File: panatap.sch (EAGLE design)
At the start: 23 parts, among them Q1 J310, Q2 BFS17, X1 IF_IN, X2 RF_OUT

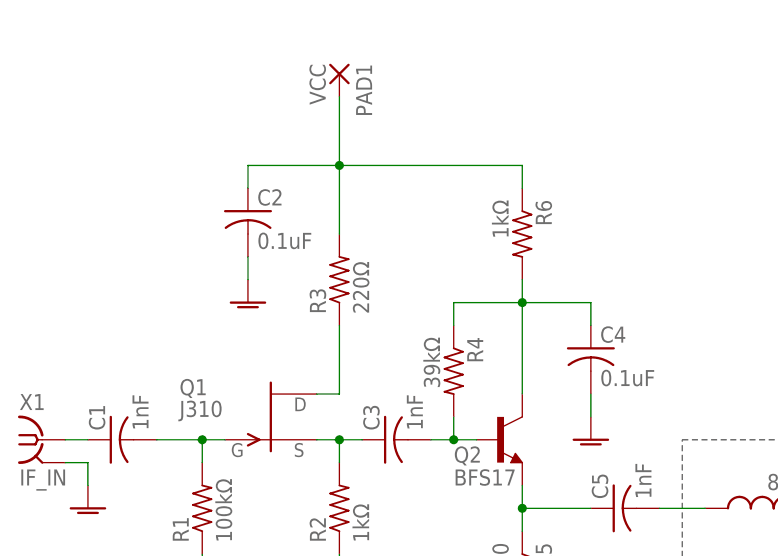
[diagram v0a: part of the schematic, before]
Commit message: Updated schematic and board with revised capacitor placement
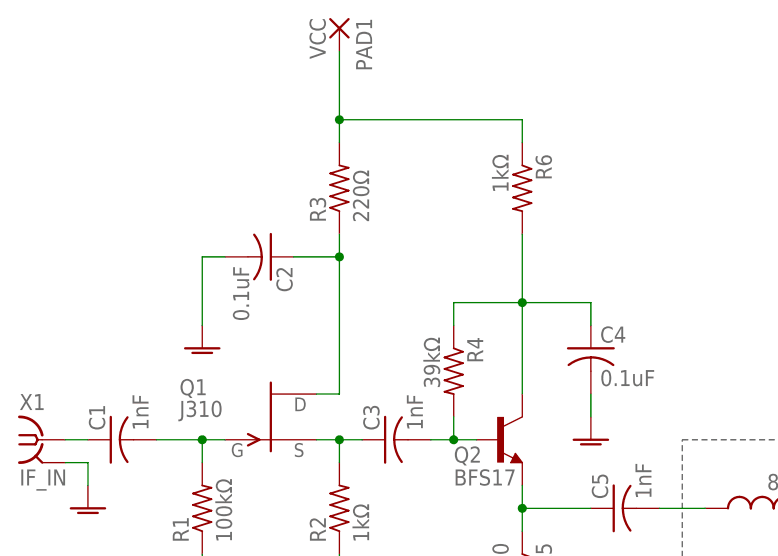
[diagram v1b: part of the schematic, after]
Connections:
- net N$8: no longer C2.1
- net N$9: now also C2.1
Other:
- moved on the sheet: C2, PAD1, R3, R6
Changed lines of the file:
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@@
 <instance part="C5" gate="G$1" x="76.2" y="45.72" rot="R90"/>
 <instance part="GND1" gate="1" x="30.48" y="35.56" smashed="yes"/>
-<instance part="PAD1" gate="G$1" x="45.72" y="93.98" rot="R270"/>
-<instance part="R3" gate="G$1" x="45.72" y="71.12" rot="R90"/>
-<instance part="C2" gate="G$1" x="35.56" y="78.74"/>
-<instance part="GND2" gate="1" x="35.56" y="68.58" smashed="yes"/>
+<instance part="PAD1" gate="G$1" x="45.72" y="99.06" rot="R270"/>
+<instance part="R3" gate="G$1" x="45.72" y="81.28" rot="R90"/>
+<instance part="C2" gate="G$1" x="38.1" y="73.66" rot="R270"/>
+<instance part="GND2" gate="1" x="30.48" y="63.5" smashed="yes"/>
 <instance part="C4" gate="G$1" x="73.66" y="63.5"/>
 <instance part="R4" gate="G$1" x="58.42" y="60.96" rot="R270"/>
 <instance part="GND3" gate="1" x="73.66" y="53.34" smashed="yes"/>
 <instance part="GND4" gate="1" x="45.72" y="35.56" smashed="yes"/>
-<instance part="R6" gate="G$1" x="66.04" y="76.2" rot="R270"/>
+<instance part="R6" gate="G$1" x="66.04" y="81.28" rot="R270"/>
 <instance part="R5" gate="G$1" x="66.04" y="38.1" rot="R270"/>
 <instance part="GND5" gate="1" x="66.04" y="27.94" smashed="yes"/>
@@
 <net name="GNDA" class="0">
 <segment>
-<pinref part="C2" gate="G$1" pin="2"/>
-<pinref part="GND2" gate="1" pin="GNDA"/>
-<wire x1="35.56" y1="73.66" x2="35.56" y2="71.12" width="0.1524" layer="91"/>
-</segment>
-<segment>
 <pinref part="GND3" gate="1" pin="GNDA"/>
 <pinref part="C4" gate="G$1" pin="2"/>
@@
 <wire x1="144.78" y1="33.02" x2="144.78" y2="35.56" width="0.1524" layer="91" style="longdash"/>
 </segment>
+<segment>
+<pinref part="C2" gate="G$1" pin="2"/>
+<pinref part="GND2" gate="1" pin="GNDA"/>
+<wire x1="33.02" y1="73.66" x2="30.48" y2="73.66" width="0.1524" layer="91"/>
+<wire x1="30.48" y1="73.66" x2="30.48" y2="66.04" width="0.1524" layer="91"/>
+</segment>
 </net>
 <net name="N$8" class="0">
 <segment>
+<pinref part="R6" gate="G$1" pin="1"/>
+<wire x1="66.04" y1="88.9" x2="66.04" y2="86.36" width="0.1524" layer="91"/>
 <pinref part="R3" gate="G$1" pin="2"/>
 <pinref part="PAD1" gate="G$1" pin="P"/>
-<wire x1="45.72" y1="76.2" x2="45.72" y2="83.82" width="0.1524" layer="91"/>
-<pinref part="C2" gate="G$1" pin="1"/>
-<wire x1="45.72" y1="83.82" x2="45.72" y2="91.44" width="0.1524" layer="91"/>
-<wire x1="35.56" y1="81.28" x2="35.56" y2="83.82" width="0.1524" layer="91"/>
-<wire x1="35.56" y1="83.82" x2="45.72" y2="83.82" width="0.1524" layer="91"/>
-<junction x="45.72" y="83.82"/>
-<pinref part="R6" gate="G$1" pin="1"/>
-<wire x1="45.72" y1="83.82" x2="66.04" y2="83.82" width="0.1524" layer="91"/>
-<wire x1="66.04" y1="83.82" x2="66.04" y2="81.28" width="0.1524" layer="91"/>
+<wire x1="45.72" y1="86.36" x2="45.72" y2="88.9" width="0.1524" layer="91"/>
+<wire x1="45.72" y1="88.9" x2="45.72" y2="96.52" width="0.1524" layer="91"/>
+<wire x1="66.04" y1="88.9" x2="45.72" y2="88.9" width="0.1524" layer="91"/>
+<junction x="45.72" y="88.9"/>
 </segment>
 </net>
@@
 <segment>
 <pinref part="R3" gate="G$1" pin="1"/>
-<wire x1="45.72" y1="66.04" x2="45.72" y2="58.42" width="0.1524" layer="91"/>
+<wire x1="45.72" y1="76.2" x2="45.72" y2="73.66" width="0.1524" layer="91"/>
 <pinref part="Q1" gate="G$1" pin="D"/>
+<wire x1="45.72" y1="73.66" x2="45.72" y2="58.42" width="0.1524" layer="91"/>
 <wire x1="45.72" y1="58.42" x2="43.18" y2="58.42" width="0.1524" layer="91"/>
+<pinref part="C2" gate="G$1" pin="1"/>
+<wire x1="40.64" y1="73.66" x2="45.72" y2="73.66" width="0.1524" layer="91"/>
+<junction x="45.72" y="73.66"/>
 </segment>
 </net>
@@
 <junction x="66.04" y="68.58"/>
 <pinref part="R6" gate="G$1" pin="2"/>
-<wire x1="66.04" y1="71.12" x2="66.04" y2="68.58" width="0.1524" layer="91"/>
+<wire x1="66.04" y1="76.2" x2="66.04" y2="68.58" width="0.1524" layer="91"/>
 </segment>
 </net>

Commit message: filter values changed, LTSpice added
filter values changed to real, obtainable components and added LTSpice simulation file
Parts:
- C6, C8: value 59pF -> 56pF
- C7: value 69F -> 68pF
- L1, L4: value 84nH -> 82nH
- L2, L3: value 185nH -> 180nH
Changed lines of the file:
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@@
 <part name="R5" library="resistor" library_urn="urn:adsk.eagle:library:348" deviceset="R-US_" device="R1206" value="100"/>
 <part name="GND5" library="supply1" library_urn="urn:adsk.eagle:library:371" deviceset="GNDA" device=""/>
-<part name="L1" library="resistor" library_urn="urn:adsk.eagle:library:348" deviceset="L-US" device="L2012C" value="84nH"/>
-<part name="L2" library="resistor" library_urn="urn:adsk.eagle:library:348" deviceset="L-US" device="L2012C" value="185nH"/>
-<part name="C6" library="resistor" library_urn="urn:adsk.eagle:library:348" deviceset="C-US" device="C1206" value="59pF"/>
+<part name="L1" library="resistor" library_urn="urn:adsk.eagle:library:348" deviceset="L-US" device="L2012C" value="82nH"/>
+<part name="L2" library="resistor" library_urn="urn:adsk.eagle:library:348" deviceset="L-US" device="L2012C" value="180nH"/>
+<part name="C6" library="resistor" library_urn="urn:adsk.eagle:library:348" deviceset="C-US" device="C1206" value="56pF"/>
 <part name="GND7" library="supply1" library_urn="urn:adsk.eagle:library:371" deviceset="GNDA" device=""/>
-<part name="C7" library="resistor" library_urn="urn:adsk.eagle:library:348" deviceset="C-US" device="C1206" value="69F"/>
+<part name="C7" library="resistor" library_urn="urn:adsk.eagle:library:348" deviceset="C-US" device="C1206" value="68pF"/>
 <part name="GND8" library="supply1" library_urn="urn:adsk.eagle:library:371" deviceset="GNDA" device=""/>
 <part name="GND9" library="supply1" library_urn="urn:adsk.eagle:library:371" deviceset="GNDA" device=""/>
 <part name="GND10" library="supply1" library_urn="urn:adsk.eagle:library:371" deviceset="GNDA" device=""/>
-<part name="L3" library="resistor" library_urn="urn:adsk.eagle:library:348" deviceset="L-US" device="L2012C" value="185nH"/>
-<part name="C8" library="resistor" library_urn="urn:adsk.eagle:library:348" deviceset="C-US" device="C1206" value="59pF"/>
-<part name="L4" library="resistor" library_urn="urn:adsk.eagle:library:348" deviceset="L-US" device="L2012C" value="84nH"/>
+<part name="L3" library="resistor" library_urn="urn:adsk.eagle:library:348" deviceset="L-US" device="L2012C" value="180nH"/>
+<part name="C8" library="resistor" library_urn="urn:adsk.eagle:library:348" deviceset="C-US" device="C1206" value="56pF"/>
+<part name="L4" library="resistor" library_urn="urn:adsk.eagle:library:348" deviceset="L-US" device="L2012C" value="82nH"/>
 <part name="GND6" library="supply1" library_urn="urn:adsk.eagle:library:371" deviceset="GNDA" device=""/>
 </parts>
